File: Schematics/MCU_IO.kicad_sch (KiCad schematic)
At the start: 1 part, among them U3 STM32H743VIHx

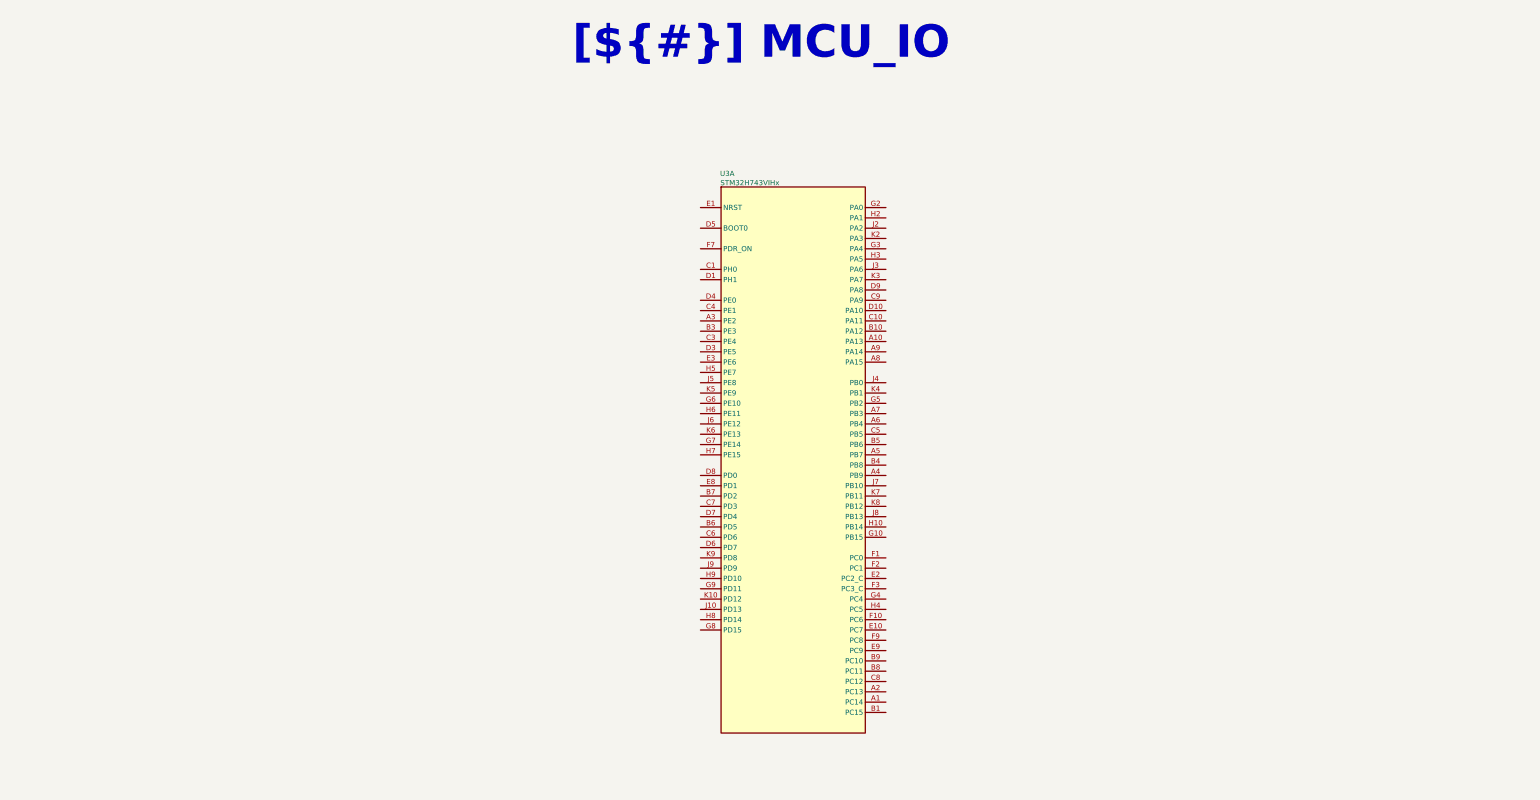
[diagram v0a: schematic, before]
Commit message: Add HSE, LSE and Programming netlabels
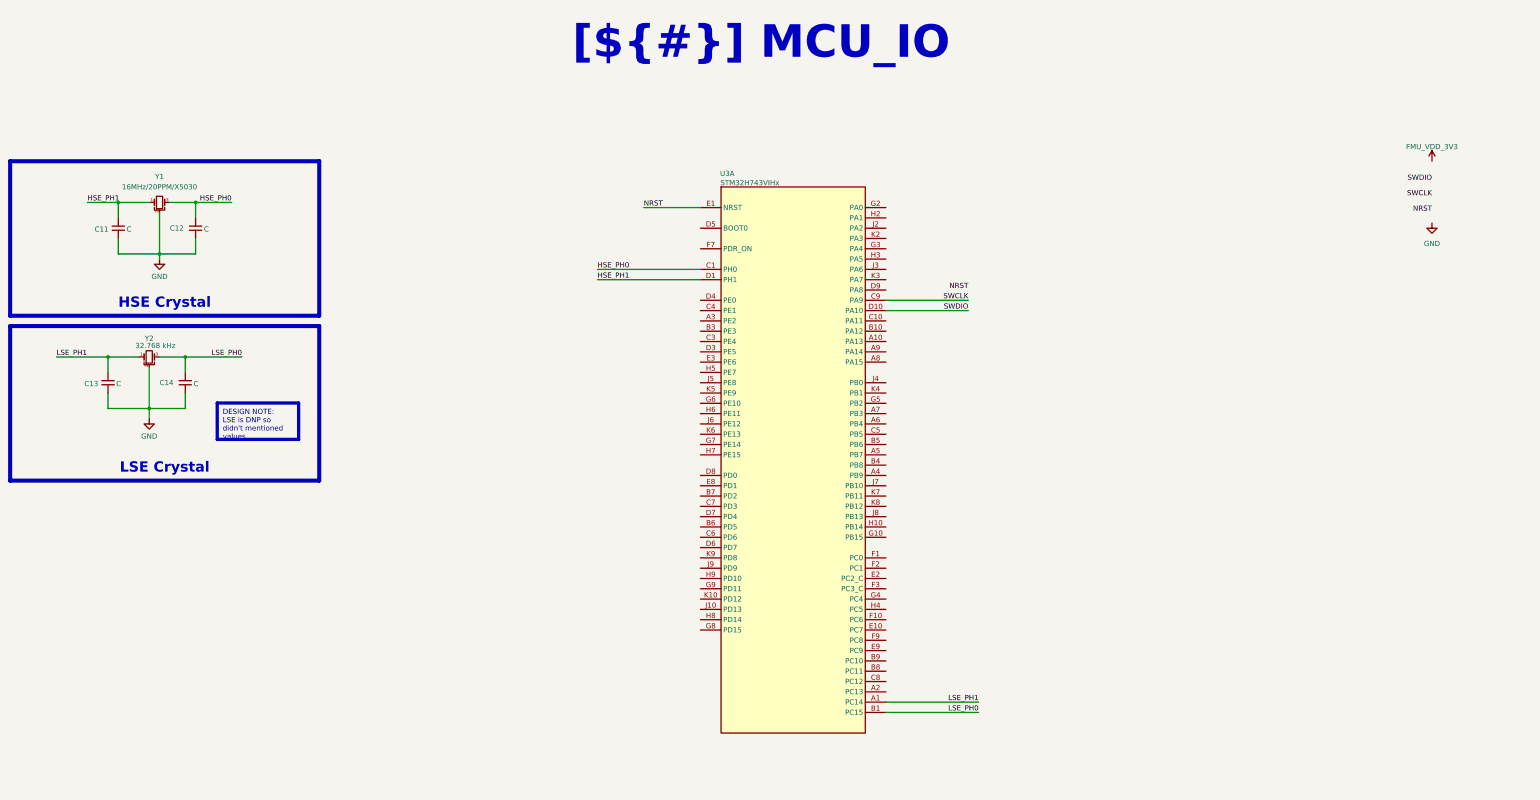
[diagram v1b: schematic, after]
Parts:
- added C11, C12, C13, C14: C, Capacitor_SMD:C_0603_1608Metric, symbol Device:C_Small
- added Y1: 16MHz/20PPM/X5030, symbol Device:Crystal_GND2_Small
- added Y2: 32.768 kHz, symbol Device:Crystal_GND2_Small
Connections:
- net LSE_PH1: now reaches U3.A1 (PC14)
- net LSE_PH1: now also C13.2, Y2.1
- net LSE_PH0: now reaches U3.B1 (PC15)
- net LSE_PH0: now also C14.2, Y2.3
- net HSE_PH0: now reaches U3.C1 (PH0)
- net HSE_PH0: now also C12.2, Y1.3
- net SWCLK: now reaches U3.C9 (PA9)
- net HSE_PH1: now reaches U3.D1 (PH1)
- net HSE_PH1: now also C11.2, Y1.1
- net SWDIO: now reaches U3.D10 (PA10)
- net NRST: now reaches U3.E1 (NRST)
- new net GND: C11.1, C12.1, C13.1, C14.1, Y1.2, Y2.2

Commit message: Add Power Conversion & Selection Ckt and SWD Debug connector
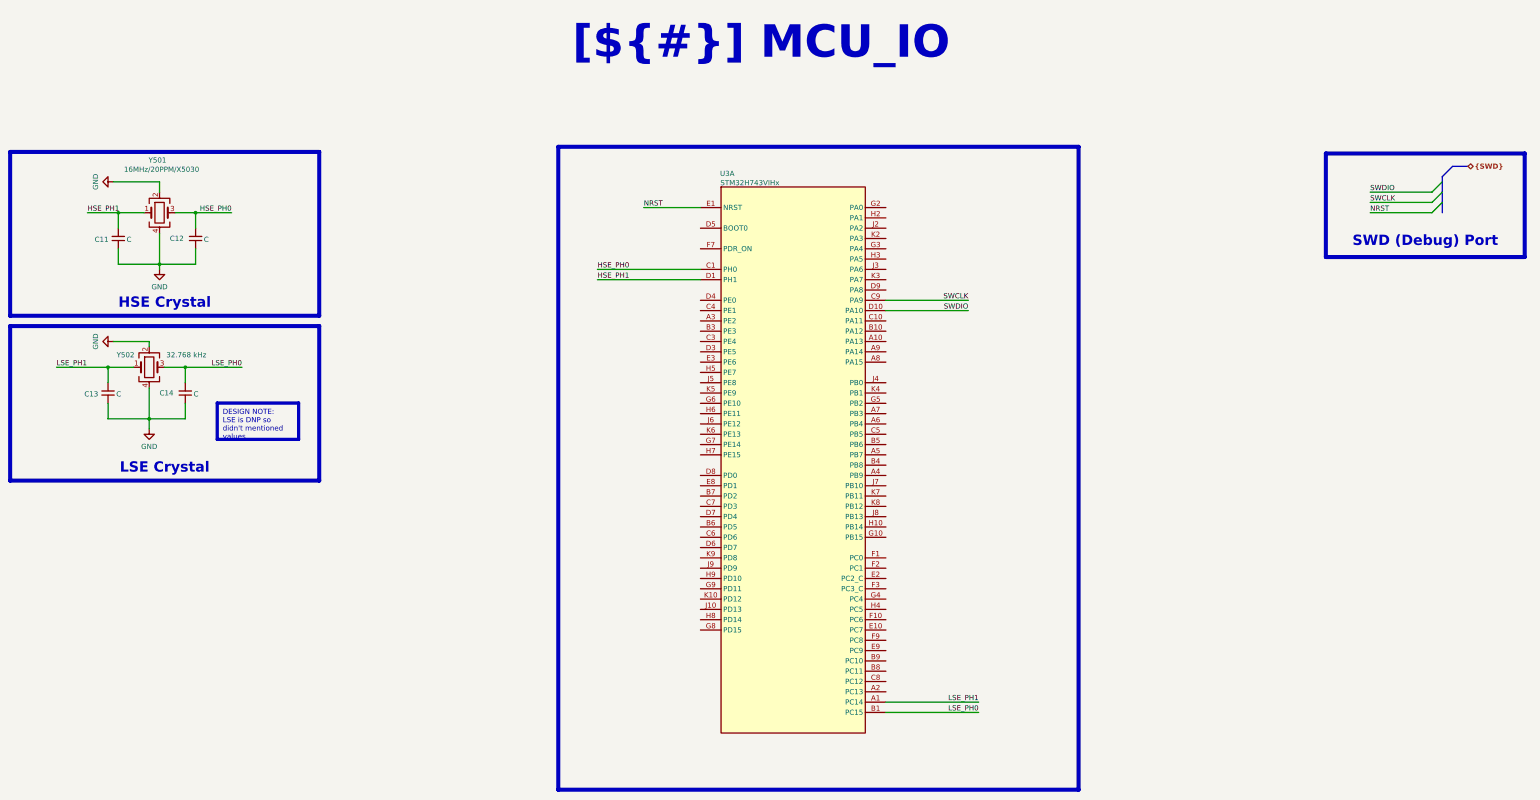
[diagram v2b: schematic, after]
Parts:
- removed Y1: 16MHz/20PPM/X5030, symbol Device:Crystal_GND2_Small
- removed Y2: 32.768 kHz, symbol Device:Crystal_GND2_Small
- added Y501: 16MHz/20PPM/X5030, Crystal:Crystal_SMD_3225-4Pin_3.2x2.5mm, symbol Device:Crystal_GND24
- added Y502: 32.768 kHz, Crystal:Crystal_SMD_3225-4Pin_3.2x2.5mm, symbol Device:Crystal_GND24
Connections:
- net GND: now also Y501.2, Y501.4, Y502.2, Y502.4
- net HSE_PH0: now also Y501.3
- net HSE_PH1: now also Y501.1
- net LSE_PH0: now also Y502.3
- net LSE_PH1: now also Y502.1
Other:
- moved on the sheet: C11, C12, C13, C14

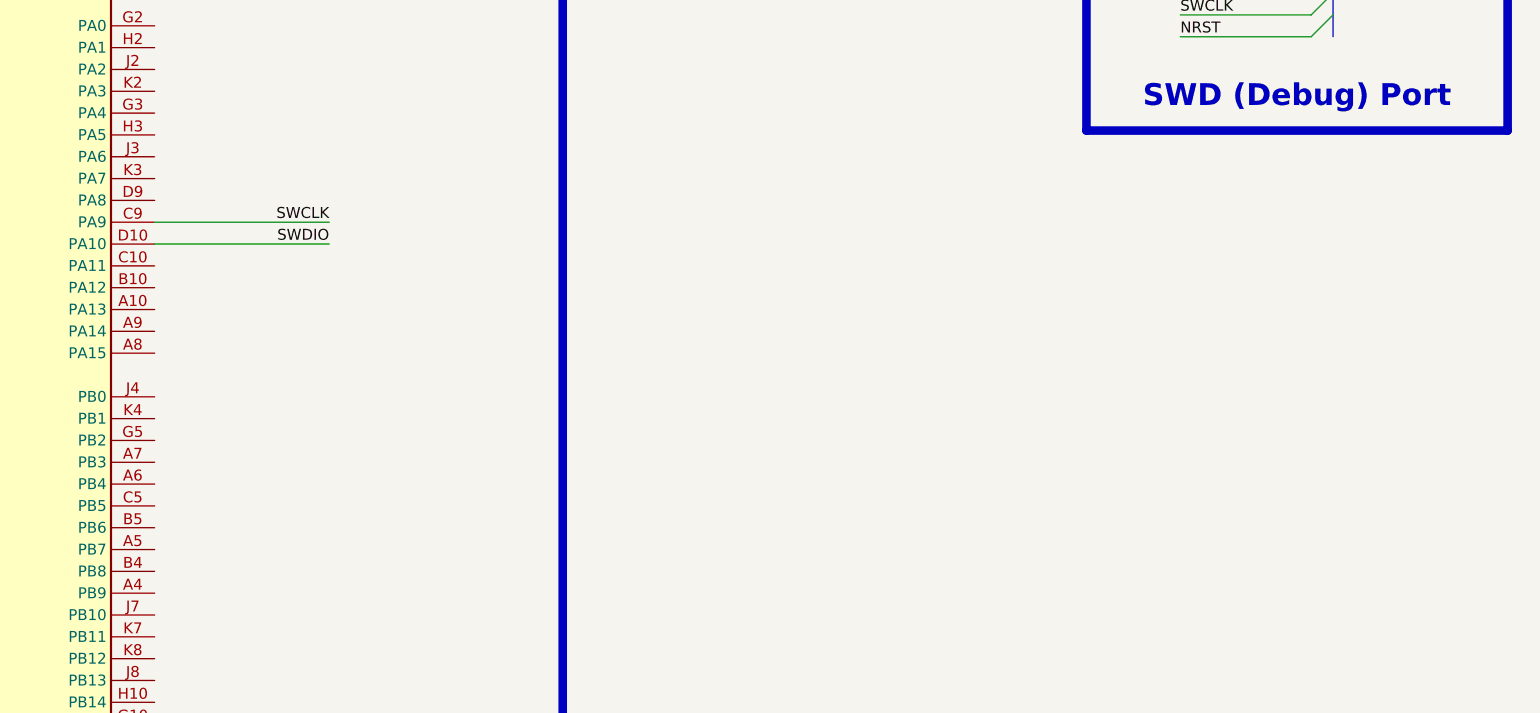
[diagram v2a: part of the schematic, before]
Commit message: Add USB
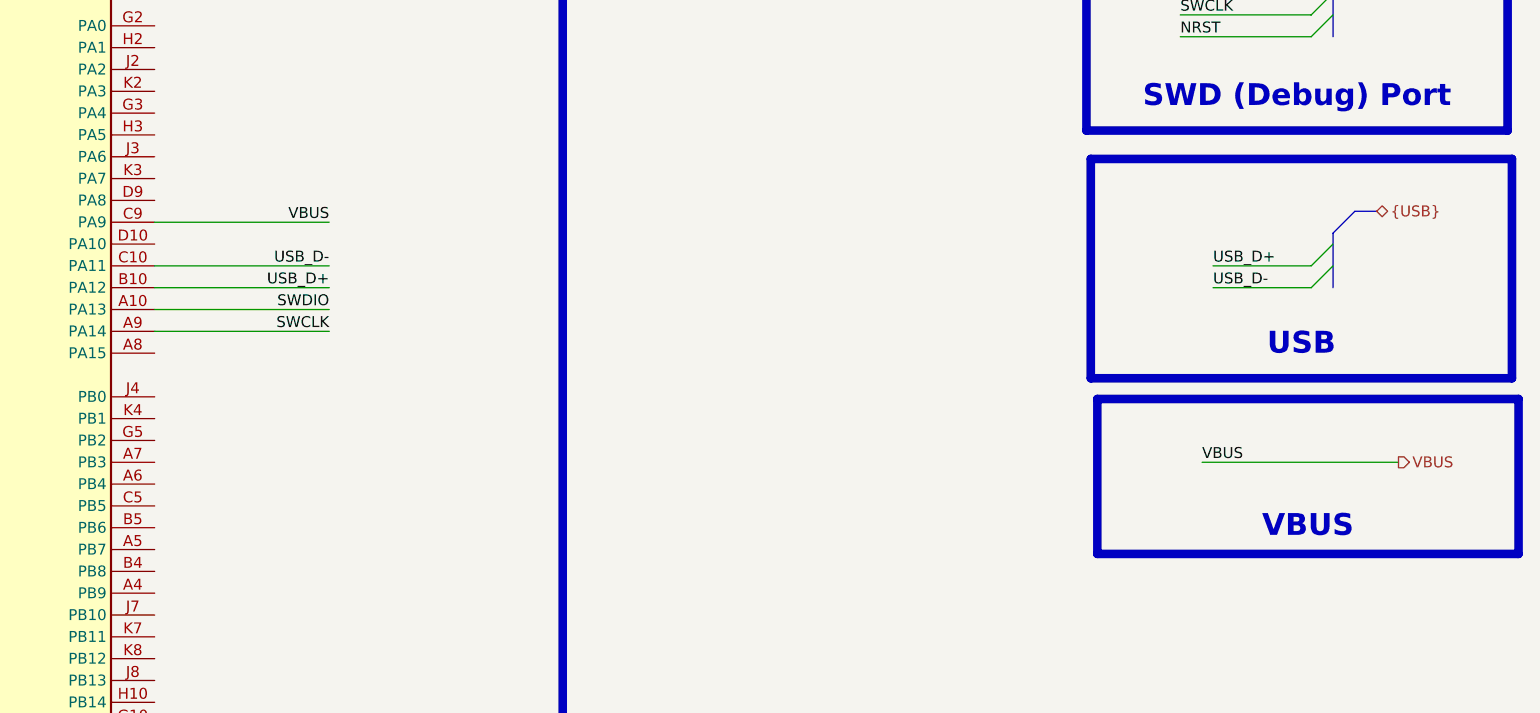
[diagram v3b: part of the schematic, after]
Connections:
- net SWCLK: now also U3.A9 (PA14); no longer U3.C9 (PA9)
- net SWDIO: now also U3.A10 (PA13); no longer U3.D10 (PA10)
- net USB_D+: now reaches U3.B10 (PA12)
- net USB_D-: now reaches U3.C10 (PA11)
- new net VBUS: U3.C9 (PA9)

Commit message: WIP
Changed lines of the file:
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@@
 	)
 	(rectangle
-		(start 349.758 104.394)
+		(start 349.25 104.394)
 		(end 398.78 122.428)
+		(stroke
+			(width 1)
+			(type default)
+			(color 200 200 200 1)
+		)
+		(fill
+			(type none)
+		)
+	)
+	(rectangle
+		(start 349.885 125.73)
+		(end 398.78 157.48)
 		(stroke
 			(width 1)
@@
 		)
 	)
+	(text_box "FRAM"
+		(exclude_from_sim no)
+		(at 349.504 149.4657 0)
+		(size 48.768 7.7603)
+		(margins 1.9049 1.9049 1.9049 1.9049)
+		(stroke
+			(width -0.0001)
+			(type solid)
+		)
+		(fill
+			(type none)
+		)
+		(effects
+			(font
+				(face "Times New Roman")
+				(size 2.54 2.54)
+				(thickness 0.508)
+				(bold yes)
+				(color 162 22 34 1)
+			)
+			(justify bottom)
+		)
+	)
 	(text_box "DESIGN NOTE:\nLSE is DNP so didn't mentioned values"
 		(exclude_from_sim no)
@@
 	)
 	(bus_entry
+		(at 381 138.43)
+		(size -2.54 2.54)
+		(stroke
+			(width 0)
+			(type default)
+		)
+	)
+	(bus_entry
+		(at 381 135.89)
+		(size -2.54 2.54)
+		(stroke
+			(width 0)
+			(type default)
+		)
+	)
+	(bus_entry
 		(at 377.19 54.61)
 		(size -2.54 2.54)
@@
 	)
 	(bus_entry
+		(at 381 143.51)
+		(size -2.54 2.54)
+		(stroke
+			(width 0)
+			(type default)
+		)
+	)
+	(bus_entry
+		(at 381 140.97)
+		(size -2.54 2.54)
+		(stroke
+			(width 0)
+			(type default)
+		)
+	)
+	(bus_entry
 		(at 377.19 59.69)
 		(size -2.54 2.54)
@@
 		)
 	)
+	(bus
+		(pts
+			(xy 381 143.51) (xy 381 146.05)
+		)
+		(stroke
+			(width 0)
+			(type default)
+		)
+	)
 	(wire
 		(pts
@@
 		)
 	)
+	(wire
+		(pts
+			(xy 354.33 138.43) (xy 378.46 138.43)
+		)
+		(stroke
+			(width 0)
+			(type default)
+		)
+	)
 	(bus
 		(pts
@@
 		)
 	)
+	(bus
+		(pts
+			(xy 383.54 132.08) (xy 381 134.62)
+		)
+		(stroke
+			(width 0)
+			(type default)
+		)
+	)
 	(wire
 		(pts
@@
 	(bus
 		(pts
+			(xy 386.08 132.08) (xy 383.54 132.08)
+		)
+		(stroke
+			(width 0)
+			(type default)
+		)
+	)
+	(bus
+		(pts
 			(xy 377.19 57.15) (xy 377.19 62.23)
 		)
@@
 	(wire
 		(pts
+			(xy 354.33 143.51) (xy 378.46 143.51)
+		)
+		(stroke
+			(width 0)
+			(type default)
+		)
+	)
+	(wire
+		(pts
 			(xy 58.42 115.57) (xy 58.42 113.03)
 		)
@@
 	(wire
 		(pts
+			(xy 354.33 140.97) (xy 378.46 140.97)
+		)
+		(stroke
+			(width 0)
+			(type default)
+		)
+	)
+	(wire
+		(pts
 			(xy 361.95 111.76) (xy 384.81 111.76)
 		)
@@
 	(wire
 		(pts
+			(xy 354.33 146.05) (xy 378.46 146.05)
+		)
+		(stroke
+			(width 0)
+			(type default)
+		)
+	)
+	(wire
+		(pts
 			(xy 240.03 185.42) (xy 262.89 185.42)
 		)
@@
 		(pts
 			(xy 60.96 76.2) (xy 60.96 74.93)
+		)
+		(stroke
+			(width 0)
+			(type default)
+		)
+	)
+	(bus
+		(pts
+			(xy 381 134.62) (xy 381 143.51)
 		)
 		(stroke
@@
 		)
 	)
+	(label "FMU_SPI2_MISO_FRAM"
+		(at 354.33 140.97 0)
+		(effects
+			(font
+				(size 1.27 1.27)
+			)
+			(justify left bottom)
+		)
+	)
+	(label "FMU_SPI2_MOSI_FRAM"
+		(at 354.33 138.43 0)
+		(effects
+			(font
+				(size 1.27 1.27)
+			)
+			(justify left bottom)
+		)
+	)
 	(label "HSE_PH0"
 		(at 168.91 76.2 0)
@@
 		)
 	)
+	(label "FMU_SPI2_CS_FRAM"
+		(at 354.33 143.51 0)
+		(effects
+			(font
+				(size 1.27 1.27)
+			)
+			(justify left bottom)
+		)
+	)
 	(label "HSE_PH0"
 		(at 78.74 62.23 180)
@@
 	(label "USB_D+"
 		(at 363.22 88.9 0)
+		(effects
+			(font
+				(size 1.27 1.27)
+			)
+			(justify left bottom)
+		)
+	)
+	(label "FMU_SPI2_SCK_FRAM"
+		(at 354.33 146.05 0)
 		(effects
 			(font
@@
 			)
 			(justify left)
+		)
+	)
+	(hierarchical_label "{FRAM}"
+		(shape bidirectional)
+		(at 386.08 132.08 0)
+		(effects
+			(font
+				(size 1.27 1.27)
+			)
+			(justify left)
